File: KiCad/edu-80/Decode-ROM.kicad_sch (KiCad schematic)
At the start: 13 parts, among them U10 7442, U4 EPROM-2708, U5 2708_(2716), U6 6116_RAM, U7 EPROM-2708, U8 PAL-003, U9 7442

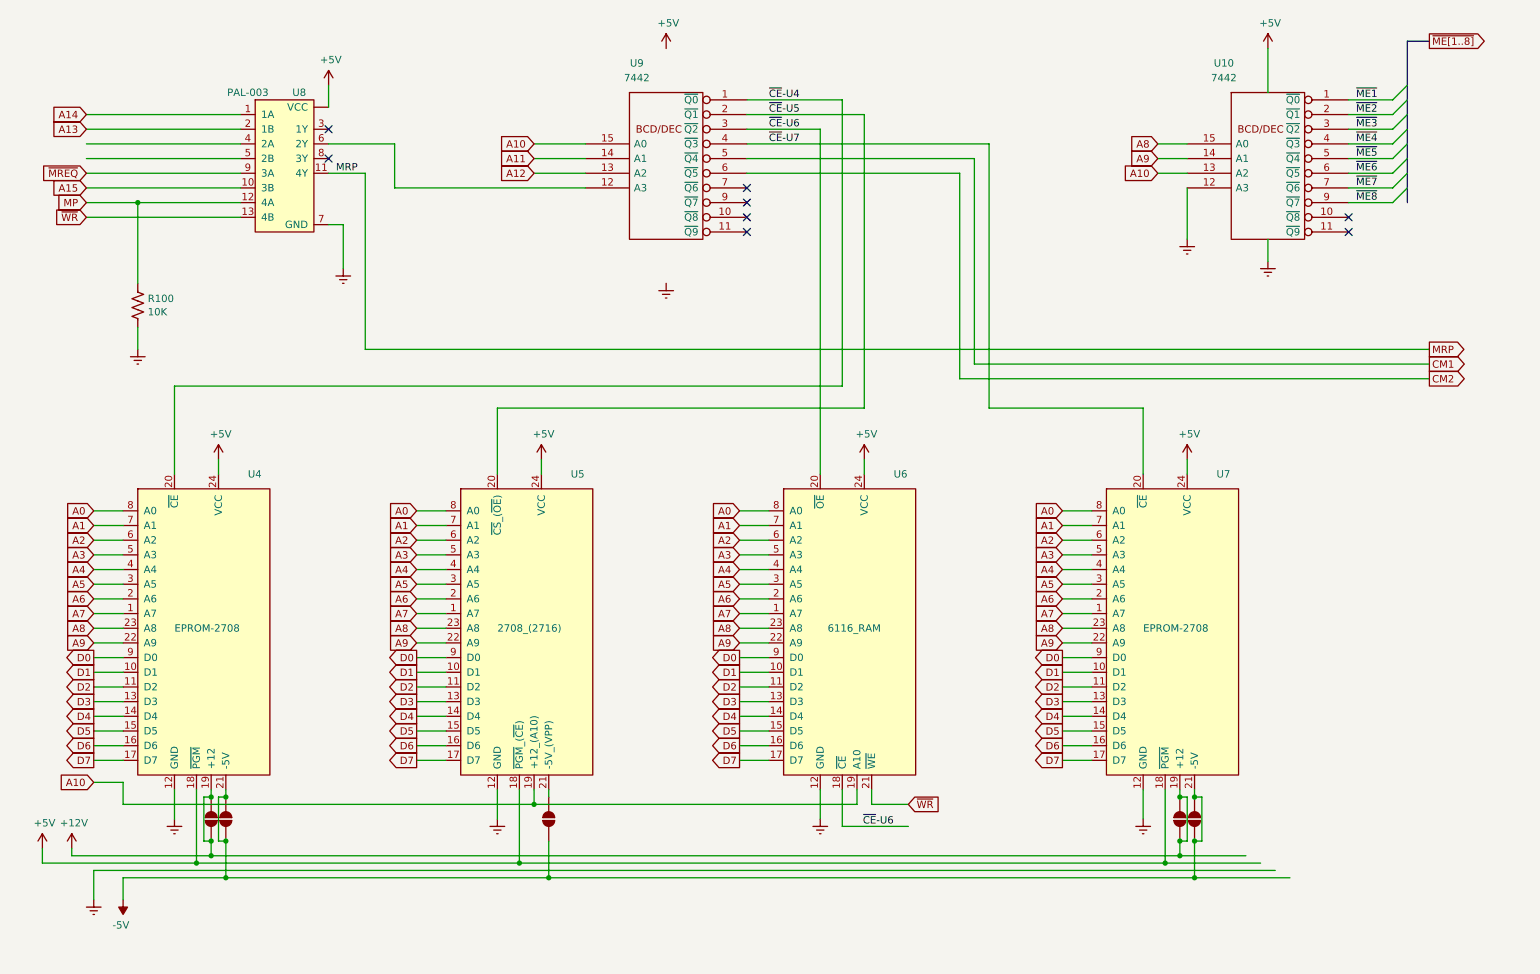
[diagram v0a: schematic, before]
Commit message: Fixed lst of the errors, still two warnings
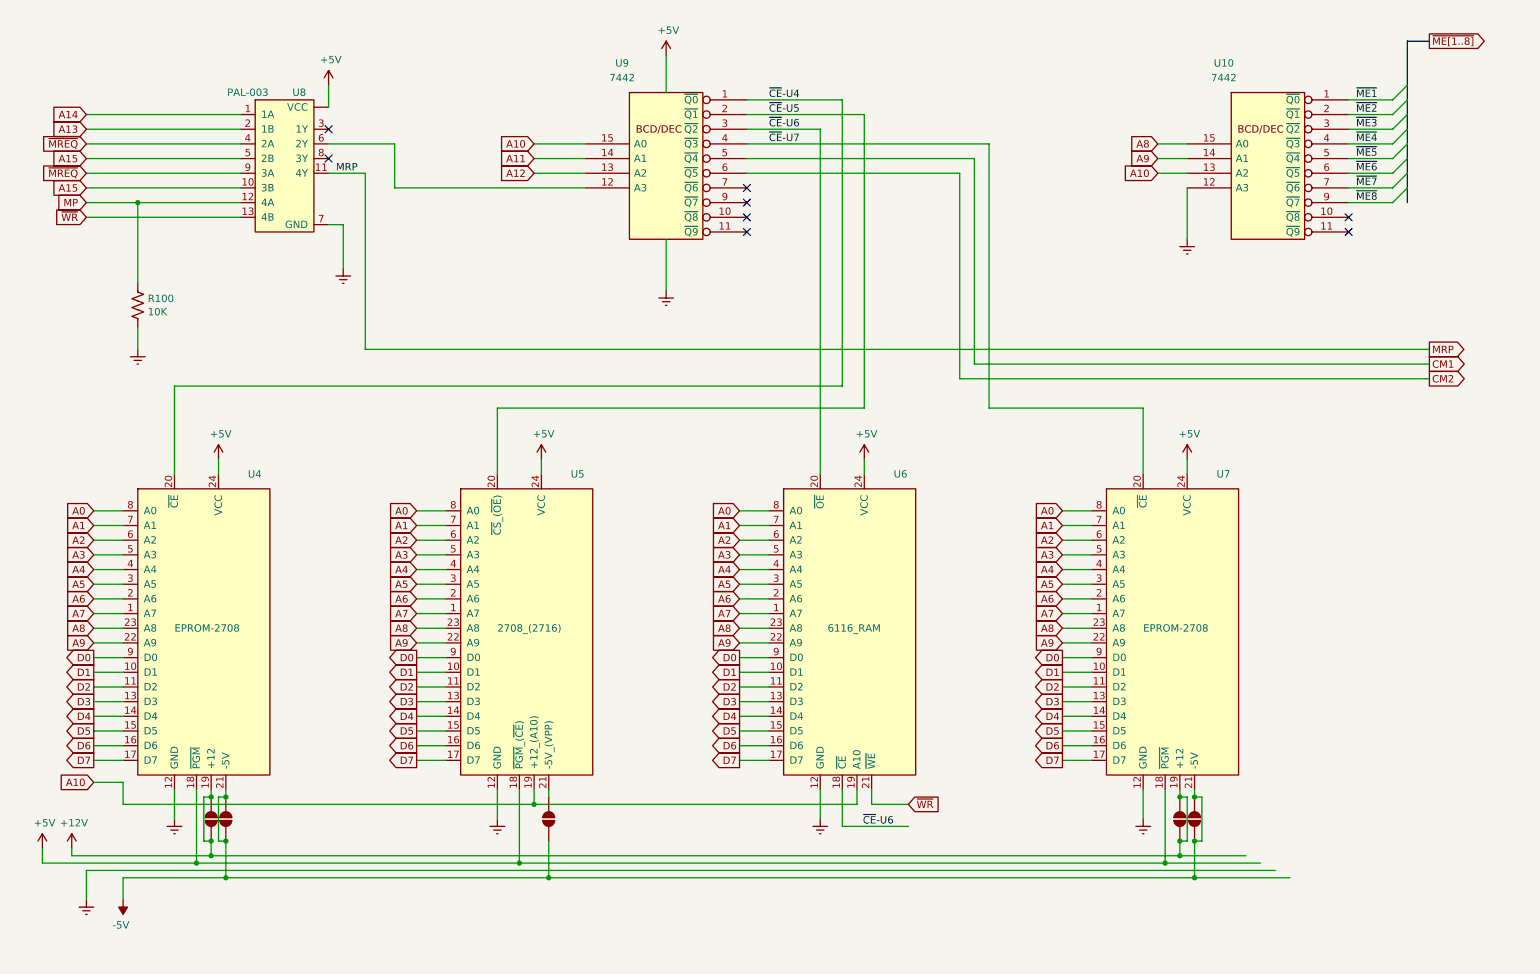
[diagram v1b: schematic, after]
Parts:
- removed U10: 7442, Package_DIP:DIP-16_W7.62mm, symbol edu-80-rescue:7442-74xx_IEEE
- removed U9: 7442, symbol edu-80-rescue:7442-74xx_IEEE
- added U10, U9: 7442, symbol Edu-80_Symbols:7442
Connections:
- net +5V: now also U10.16 (VCC), U9.16 (VCC)
- net A10: now also U10.13 (A2), U9.15 (A0)
- net A11: now also U9.14 (A1)
- net A12: now also U9.13 (A2)
- net A15: now also U8.5 (2B)
- net A8: now also U10.15 (A0)
- net A9: now also U10.14 (A1)
- net CM1: now also U9.5 (~{Q4})
- net CM2: now also U9.6 (~{Q5})
- net Earth: now also U10.12 (A3), U10.8 (GND), U9.8 (GND)
- net ~{CE}-U4: now also U9.1 (~{Q0})
- net ~{CE}-U5: now also U9.2 (~{Q1})
- net ~{CE}-U6: now also U9.3 (~{Q2})
- net ~{CE}-U7: now also U9.4 (~{Q3})
- net ~{ME1}: now also U10.1 (~{Q0})
- net ~{ME2}: now also U10.2 (~{Q1})
- net ~{ME3}: now also U10.3 (~{Q2})
- net ~{ME4}: now also U10.4 (~{Q3})
- net ~{ME5}: now also U10.5 (~{Q4})
- net ~{ME6}: now also U10.6 (~{Q5})
- net ~{ME7}: now also U10.7 (~{Q6})
- net ~{ME8}: now also U10.9 (~{Q7})
- net ~{MREQ}: now also U8.4 (2A)
- net at U8.6 (2Y): now also U9.12 (A3)

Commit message: Working on removing edu-80-rescue symbol library
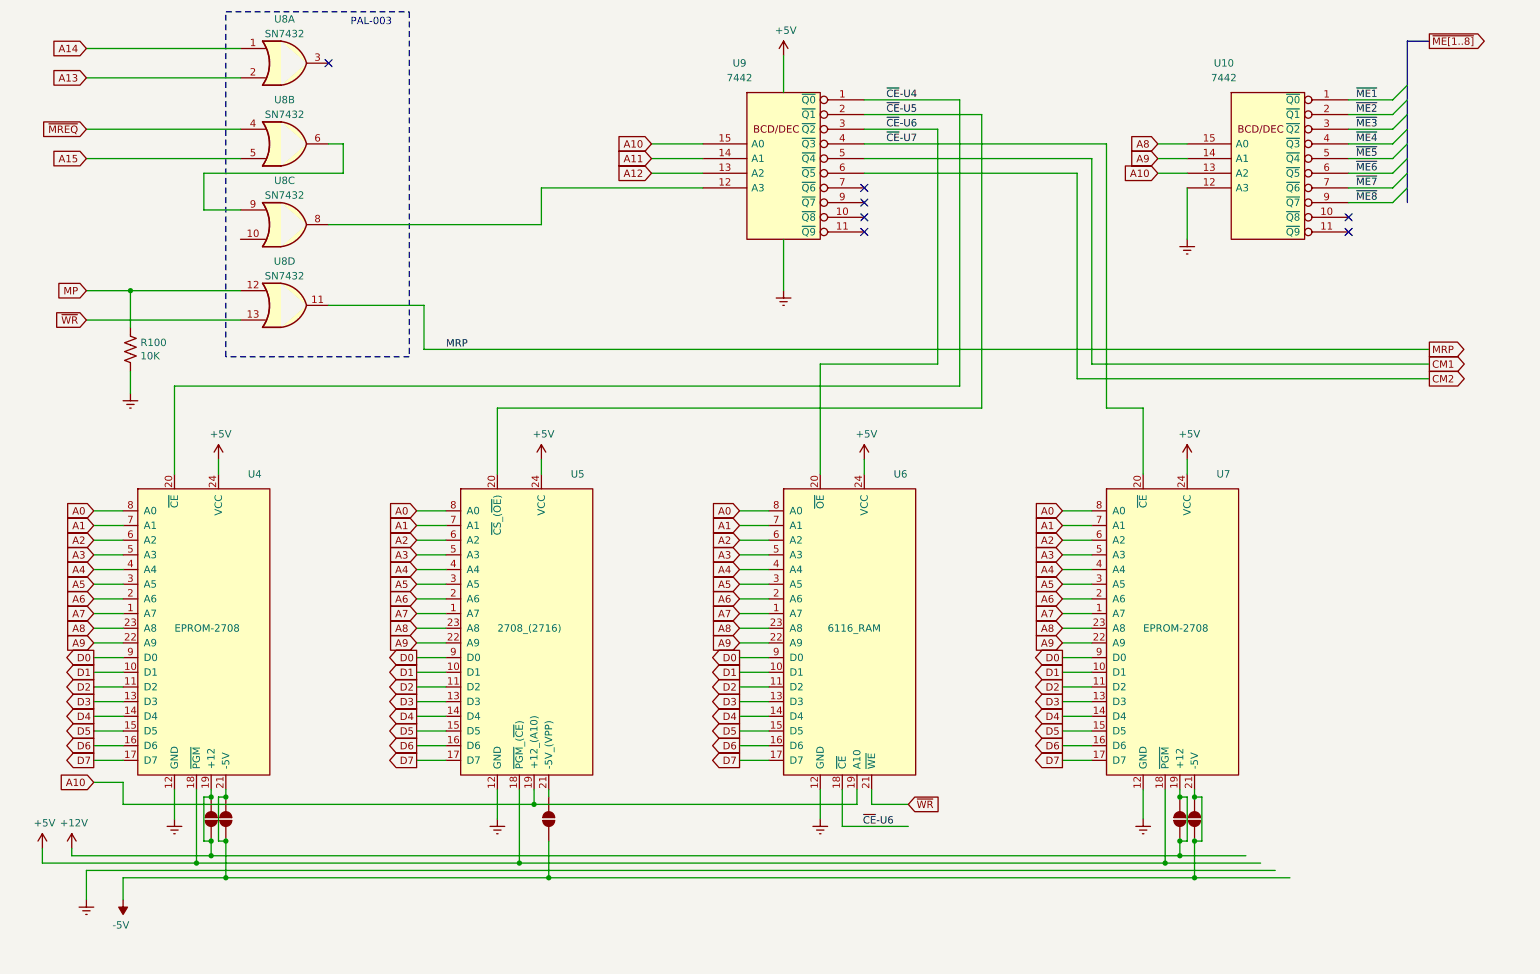
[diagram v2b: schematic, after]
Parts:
- removed U8: PAL-003, symbol edu-80-rescue:PAL-003-Edu-80_Symbol
- added U8: SN7432, symbol Edu-80_Symbols:SN7432
- U6: symbol edu-80-rescue:6116_RAM-Edu-80_Symbol -> Edu-80_Symbols:6116_RAM
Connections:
- net A13: now also U8.2
- net A14: now also U8.1
- net A15: now also U8.5
- net MP: now also U8.12
- net MRP: now also U8.11
- net ~{MREQ}: now also U8.4
- net ~{WR}: now also U8.13
- net at U9.12 (A3): now also U8.8
- new net: U8.6, U8.9
- no-connect marks 8 -> 7
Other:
- note added: "PAL-003"
- moved on the sheet: R100, U9

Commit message: Cleaning up the PAL-003 decoding, adding Modifications page.
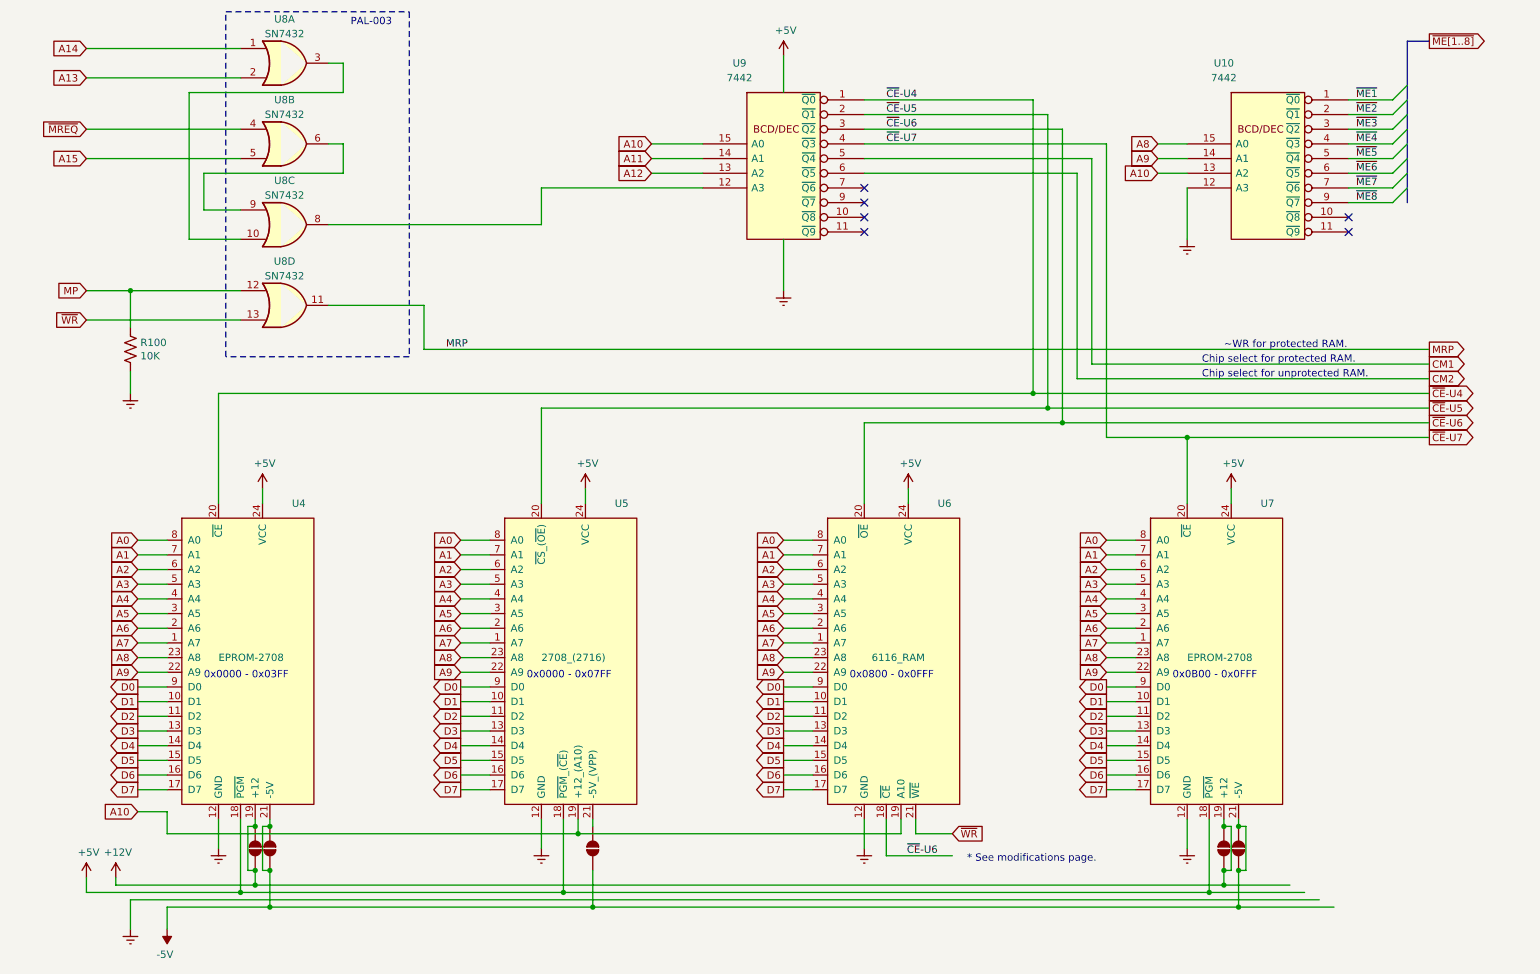
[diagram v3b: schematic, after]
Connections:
- net at U8.10: now also U8.3
- no-connect marks 7 -> 6
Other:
- note added: "* See modifications page."
- note added: "0x0000 - 0x03FF"
- note added: "0x0000 - 0x07FF"
- note added: "0x0800 - 0x0FFF"
- note added: "0x0B00 - 0x0FFF"
- note added: "Chip select for protected RAM."
- note added: "Chip select for unprotected RAM."
- note added: "~WR for protected RAM."
- moved on the sheet: U4, U5, U6, U7
